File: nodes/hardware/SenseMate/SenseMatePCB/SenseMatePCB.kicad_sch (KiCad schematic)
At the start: 16 parts, among them M1 Motor_DC, Q1 2SC1815, Q2 2SC1815, SW1 SW_Push, SW2 SW_Push, SW3 SW_Push, SW5 SW_DPDT_x2

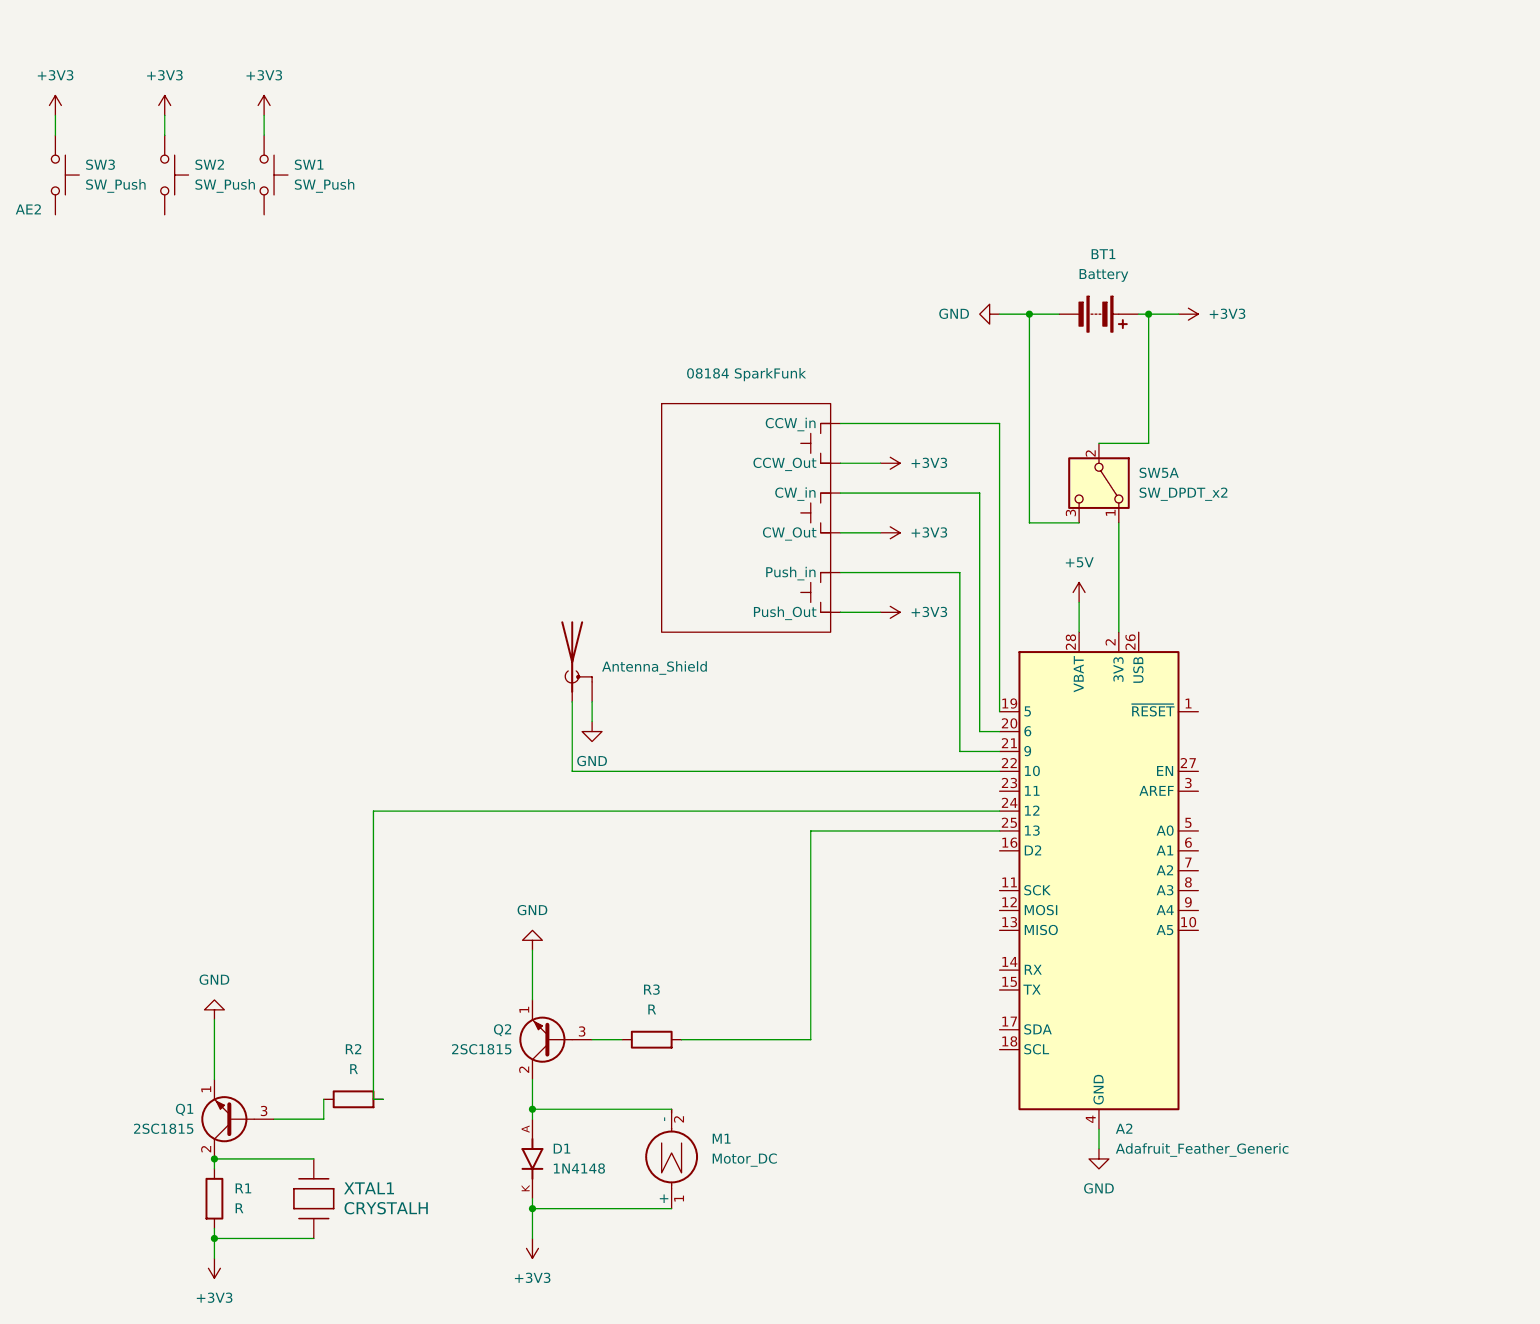
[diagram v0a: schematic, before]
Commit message: added Display and Lora Lables
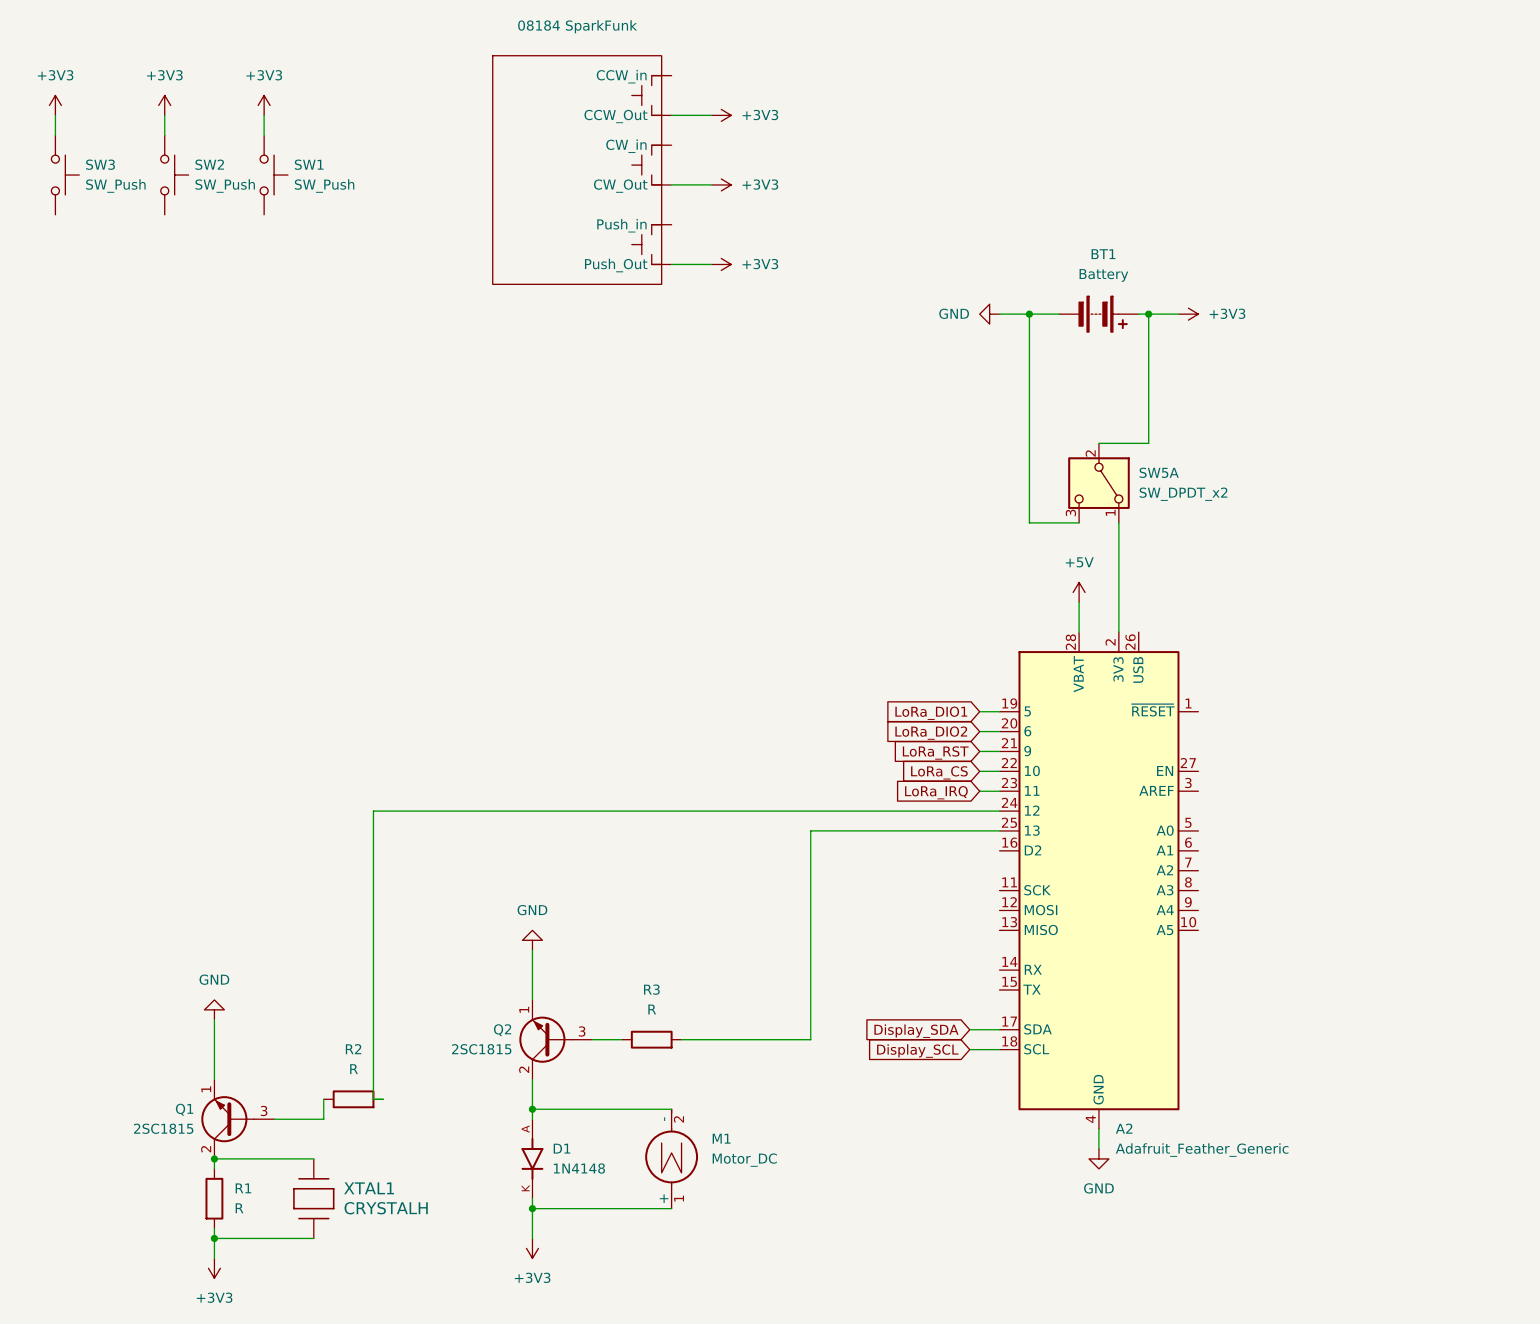
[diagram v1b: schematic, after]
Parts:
- removed AE2: Antenna_Shield, symbol Device:Antenna_Shield
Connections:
- net LoRa_DIO1: now reaches A2.19 (5)
- net LoRa_DIO1: no longer 08184 SparkFunk. (Push_Out)
- net LoRa_DIO2: now reaches A2.20 (6)
- net LoRa_DIO2: no longer 08184 SparkFunk. (Push_Out)
- net LoRa_RST: now reaches A2.21 (9)
- net LoRa_RST: no longer 08184 SparkFunk. (Push_Out)
- net LoRa_CS: now reaches A2.22 (10)
- net Display_SDA: now reaches A2.17 (SDA)
- net Display_SCL: now reaches A2.18 (SCL)
- net LoRa_IRQ: now reaches A2.23 (11)
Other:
- moved on the sheet: 08184 SparkFunk

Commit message: first draft for schematic finished and ready for testing
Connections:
- net +5V is gone; now on an unnamed net: A2.28 (VBAT)
- net +3V3: now also A2.2 (3V3); no longer BT1.1 (+), SW5.2 (B)
- net GND: no longer SW5.3 (C)
- net at SW5.1 (A): no longer A2.2 (3V3)
- new net: BT1.1 (+), SW5.2 (B)
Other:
- moved on the sheet: BT1, SW5A
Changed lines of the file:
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@@
-	)
-	(junction
-		(at 193.04 48.26)
-		(diameter 0)
-		(color 0 0 0 0)
 	)
 	(junction
@@
 	)
 	(junction
-		(at 208.28 48.26)
-		(diameter 0)
-		(color 0 0 0 0)
-	)
-	(junction
 		(at 129.54 162.56)
 		(diameter 0)
@@
 	(wire
 		(pts
-			(xy 193.04 74.93) (xy 193.04 48.26)
-		)
-		(stroke
-			(width 0)
-			(type default)
-		)
-	)
-	(wire
-		(pts
 			(xy 186.69 104.14) (xy 189.23 104.14)
 		)
@@
 	(wire
 		(pts
-			(xy 208.28 64.77) (xy 208.28 48.26)
+			(xy 203.2 71.12) (xy 203.2 54.61)
 		)
 		(stroke
@@
 	(wire
 		(pts
-			(xy 199.39 74.93) (xy 193.04 74.93)
-		)
-		(stroke
-			(width 0)
-			(type default)
-		)
-	)
-	(wire
-		(pts
 			(xy 147.32 22.86) (xy 152.4 22.86)
 		)
@@
 	(wire
 		(pts
-			(xy 201.93 64.77) (xy 208.28 64.77)
+			(xy 196.85 71.12) (xy 203.2 71.12)
 		)
 		(stroke
@@
 	(wire
 		(pts
-			(xy 207.01 48.26) (xy 208.28 48.26)
+			(xy 201.93 54.61) (xy 203.2 54.61)
 		)
 		(stroke
@@
 	(wire
 		(pts
+			(xy 204.47 86.36) (xy 204.47 88.9)
+		)
+		(stroke
+			(width 0)
+			(type default)
+		)
+	)
+	(wire
+		(pts
 			(xy 186.69 99.06) (xy 189.23 99.06)
 		)
@@
 	(wire
 		(pts
-			(xy 193.04 48.26) (xy 196.85 48.26)
-		)
-		(stroke
-			(width 0)
-			(type default)
-		)
-	)
-	(wire
-		(pts
-			(xy 199.39 85.09) (xy 199.39 88.9)
+			(xy 184.15 54.61) (xy 191.77 54.61)
+		)
+		(stroke
+			(width 0)
+			(type default)
+		)
+	)
+	(wire
+		(pts
+			(xy 199.39 81.28) (xy 199.39 88.9)
 		)
 		(stroke
@@
 	(wire
 		(pts
-			(xy 189.23 48.26) (xy 193.04 48.26)
-		)
-		(stroke
-			(width 0)
-			(type default)
-		)
-	)
-	(wire
-		(pts
 			(xy 186.69 106.68) (xy 189.23 106.68)
 		)
@@
 		(pts
 			(xy 129.54 129.54) (xy 129.54 135.89)
-		)
-		(stroke
-			(width 0)
-			(type default)
-		)
-	)
-	(wire
-		(pts
-			(xy 204.47 74.93) (xy 204.47 88.9)
-		)
-		(stroke
-			(width 0)
-			(type default)
-		)
-	)
-	(wire
-		(pts
-			(xy 208.28 48.26) (xy 212.09 48.26)
 		)
 		(stroke
@@
 	(symbol
 		(lib_id "Switch:SW_DPDT_x2")
-		(at 201.93 69.85 270)
+		(at 196.85 76.2 270)
 		(unit 1)
 		(exclude_from_sim no)
@@
 		(fields_autoplaced yes)
 		(property "Reference" "SW5"
-			(at 207.01 68.5799 90)
+			(at 201.93 74.9299 90)
 			(effects
 				(font
@@
 		)
 		(property "Value" "SW_DPDT_x2"
-			(at 207.01 71.1199 90)
+			(at 201.93 77.4699 90)
 			(effects
 				(font
@@
 		)
 		(property "Footprint" ""
-			(at 201.93 69.85 0)
+			(at 196.85 76.2 0)
 			(effects
 				(font
@@
 		)
 		(property "Datasheet" "~"
-			(at 201.93 69.85 0)
+			(at 196.85 76.2 0)
 			(effects
 				(font
@@
 		)
 		(property "Description" "Switch, dual pole double throw, separate symbols"
-			(at 201.93 69.85 0)
+			(at 196.85 76.2 0)
 			(effects
 				(font
@@
 	(symbol
 		(lib_id "power:+3V3")
-		(at 212.09 48.26 270)
-		(unit 1)
-		(exclude_from_sim no)
-		(in_bom yes)
-		(on_board yes)
-		(dnp no)
-		(fields_autoplaced yes)
+		(at 204.47 86.36 0)
+		(unit 1)
+		(exclude_from_sim no)
+		(in_bom yes)
+		(on_board yes)
+		(dnp no)
 		(property "Reference" "#PWR01"
-			(at 208.28 48.26 0)
+			(at 204.47 90.17 0)
 			(effects
 				(font
@@
 		)
 		(property "Value" "+3V3"
-			(at 215.9 48.2599 90)
+			(at 201.422 82.296 0)
 			(effects
 				(font
@@
 		)
 		(property "Footprint" ""
-			(at 212.09 48.26 0)
+			(at 204.47 86.36 0)
 			(effects
 				(font
@@
 		)
 		(property "Datasheet" ""
-			(at 212.09 48.26 0)
+			(at 204.47 86.36 0)
 			(effects
 				(font
@@
 		)
 		(property "Description" "Power symbol creates a global label with name \"+3V3\""
-			(at 212.09 48.26 0)
+			(at 204.47 86.36 0)
 			(effects
 				(font
@@
 	)
 	(symbol
-		(lib_id "power:+5V")
-		(at 199.39 85.09 0)
-		(unit 1)
-		(exclude_from_sim no)
-		(in_bom yes)
-		(on_board yes)
-		(dnp no)
-		(fields_autoplaced yes)
-		(property "Reference" "#PWR03"
-			(at 199.39 88.9 0)
-			(effects
-				(font
-					(size 1.27 1.27)
-				)
-				(hide yes)
-			)
-		)
-		(property "Value" "+5V"
-			(at 199.39 80.01 0)
-			(effects
-				(font
-					(size 1.27 1.27)
-				)
-			)
-		)
-		(property "Footprint" ""
-			(at 199.39 85.09 0)
-			(effects
-				(font
-					(size 1.27 1.27)
-				)
-				(hide yes)
-			)
-		)
-		(property "Datasheet" ""
-			(at 199.39 85.09 0)
-			(effects
-				(font
-					(size 1.27 1.27)
-				)
-				(hide yes)
-			)
-		)
-		(property "Description" "Power symbol creates a global label with name \"+5V\""
-			(at 199.39 85.09 0)
-			(effects
-				(font
-					(size 1.27 1.27)
-				)
-				(hide yes)
-			)
-		)
-		(pin "1"
-		)
-		(instances
-			(project ""
-				(path "/70e40189-008f-4f72-8f4c-fe289f3548a4"
-					(reference "#PWR03")
-					(unit 1)
-				)
-			)
-		)
-	)
-	(symbol
 		(lib_id "SenseMateLibrary:Adafruit_Feather_Generic")
 		(at 201.93 119.38 0)
@@
 	(symbol
 		(lib_id "Device:Battery")
-		(at 201.93 48.26 270)
+		(at 196.85 54.61 270)
 		(unit 1)
 		(exclude_from_sim no)
@@
 		(fields_autoplaced yes)
 		(property "Reference" "BT1"
-			(at 202.5015 40.64 90)
+			(at 197.4215 46.99 90)
 			(effects
 				(font
@@
 		)
 		(property "Value" "Battery"
-			(at 202.5015 43.18 90)
+			(at 197.4215 49.53 90)
 			(effects
 				(font
@@
 		)
 		(property "Footprint" ""
-			(at 203.454 48.26 90)
+			(at 198.374 54.61 90)
 			(effects
 				(font
@@
 		)
 		(property "Datasheet" "~"
-			(at 203.454 48.26 90)
+			(at 198.374 54.61 90)
 			(effects
 				(font
@@
 		)
 		(property "Description" "Multiple-cell battery"
-			(at 201.93 48.26 0)
+			(at 196.85 54.61 0)
 			(effects
 				(font
@@
 	(symbol
 		(lib_id "power:GND")
-		(at 189.23 48.26 270)
+		(at 184.15 54.61 270)
 		(unit 1)
 		(exclude_from_sim no)
@@
 		(fields_autoplaced yes)
 		(property "Reference" "#PWR012"
-			(at 182.88 48.26 0)
+			(at 177.8 54.61 0)
 			(effects
 				(font
@@
 		)
 		(property "Value" "GND"
-			(at 185.42 48.2599 90)
+			(at 180.34 54.6099 90)
 			(effects
 				(font
@@
 		)
 		(property "Footprint" ""
-			(at 189.23 48.26 0)
+			(at 184.15 54.61 0)
 			(effects
 				(font
@@
 		)
 		(property "Datasheet" ""
-			(at 189.23 48.26 0)
+			(at 184.15 54.61 0)
 			(effects
 				(font
@@
 		)
 		(property "Description" "Power symbol creates a global label with name \"GND\" , ground"
-			(at 189.23 48.26 0)
-			(effects
-				(font
+			(at 184.15 54.61 0)
+			(effects
+				(font

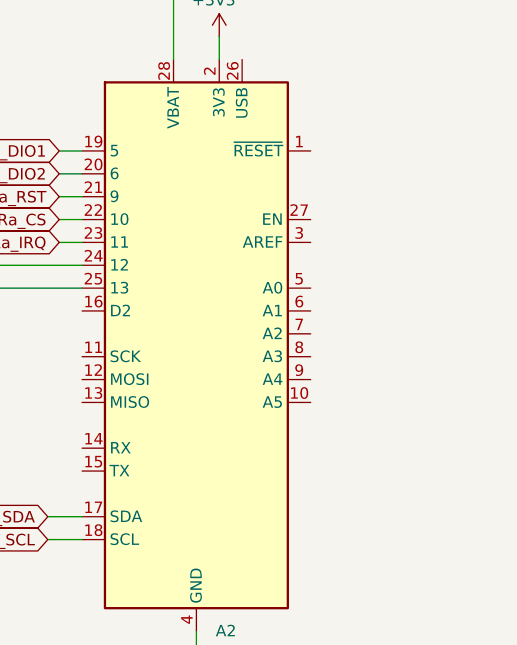
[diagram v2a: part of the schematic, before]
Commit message: somehow PushJoySTick got deleted, added again
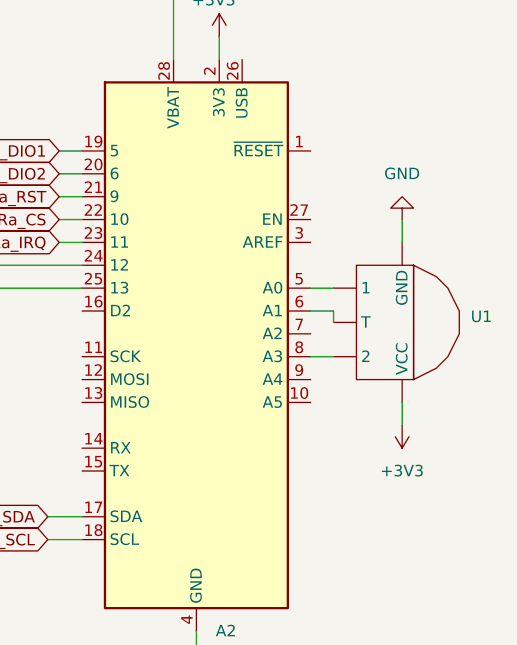
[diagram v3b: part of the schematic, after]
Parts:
- added U1: ~, symbol FeatherSense_JoyButton:08184_SparkFunk
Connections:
- net +3V3: now also U1. (VCC)
- net GND: now also U1. (VCC)
- net at A2.5 (A0): now also U1. (VCC)
- net at A2.6 (A1): now also U1. (VCC)
- net at A2.8 (A3): now also U1. (VCC)
